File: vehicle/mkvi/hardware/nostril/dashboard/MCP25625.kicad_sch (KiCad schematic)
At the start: 9 parts, among them U2 MCP25625-x-SS, Y1 Crystal_12MHz

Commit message: Final Dashboard Schematic
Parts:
- removed Y1: Crystal_12MHz, footprints:Crystal_SMD_FA238, symbol formula:Crystal_12MHz
- added Y1: Crystal_8MHz_12pF, XTAL_ECS-240-8-33-AGN-TR, symbol formula:Crystal_8MHz_12pF
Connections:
- net GND: now also Y1.2, Y1.4
- net at C7.1, U2.9 (OSC1): now also Y1.1
- net at C8.1, U2.8 (OSC2): now also Y1.3
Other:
- note removed: "Upload actual digikey part This is a placeholder crystal"
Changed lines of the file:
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@@
+    (stroke (width 0) (type default) (color 0 0 0 0))
+  )
+  (wire (pts (xy 156.845 120.015) (xy 151.13 120.015))
     (stroke (width 0) (type default) (color 0 0 0 0))
   )
@@
     (stroke (width 0) (type default) (color 0 0 0 0))
   )
-  (wire (pts (xy 158.115 120.015) (xy 151.13 120.015))
-    (stroke (width 0) (type default) (color 0 0 0 0))
-  )
   (wire (pts (xy 164.465 107.315) (xy 164.465 107.95))
     (stroke (width 0) (type default) (color 0 0 0 0))
@@
     (stroke (width 0) (type default) (color 0 0 0 0))
   )
+  (wire (pts (xy 160.655 114.935) (xy 160.655 107.315))
+    (stroke (width 0) (type default) (color 0 0 0 0))
+  )
   (wire (pts (xy 151.13 120.015) (xy 151.13 126.365))
     (stroke (width 0) (type default) (color 0 0 0 0))
@@
     (stroke (width 0) (type default) (color 0 0 0 0))
   )
-  (wire (pts (xy 160.655 116.205) (xy 160.655 107.315))
-    (stroke (width 0) (type default) (color 0 0 0 0))
-  )
   (wire (pts (xy 115.57 93.345) (xy 91.44 93.345))
     (stroke (width 0) (type default) (color 0 0 0 0))
   )
-  (wire (pts (xy 171.45 120.015) (xy 163.195 120.015))
+  (wire (pts (xy 171.45 120.015) (xy 164.465 120.015))
     (stroke (width 0) (type default) (color 0 0 0 0))
   )
@@
     (stroke (width 0) (type default) (color 0 0 0 0))
   )
-  (wire (pts (xy 160.655 123.825) (xy 160.655 133.985))
-    (stroke (width 0) (type default) (color 0 0 0 0))
-  )
   (wire (pts (xy 107.95 53.975) (xy 107.95 55.245))
     (stroke (width 0) (type default) (color 0 0 0 0))
@@
     (stroke (width 0) (type default) (color 0 0 0 0))
   )
+  (wire (pts (xy 160.655 125.095) (xy 160.655 133.985))
+    (stroke (width 0) (type default) (color 0 0 0 0))
+  )
   (wire (pts (xy 106.68 83.185) (xy 115.57 83.185))
     (stroke (width 0) (type default) (color 0 0 0 0))
-  )
-  (text "Upload actual digikey part\nThis is a placeholder crystal"
-    (at 170.815 116.205 0)
-    (effects (font (size 0.5 0.5)) (justify right bottom))
   )
   (text "Crystal: 12pF, 8 MHz\nPin Load Capacitance (assumed: 5pF)\n\nCL= C1*C2/(C1+C2)\nC1=C2\n(C1^2)/2C1 + 5pF = 12 pF\nC1 = 14 pF\n\nTo do: Add footprint for 14 pF capacitor"
@@
     (effects (font (size 1.27 1.27)) (justify right bottom))
   )
-  (label "CAN_+" (at 158.115 73.025 0)
-    (effects (font (size 1.27 1.27)) (justify left bottom))
-  )
   (label "MOSI" (at 115.57 83.185 180)
     (effects (font (size 1.27 1.27)) (justify right bottom))
@@
     (effects (font (size 1.27 1.27)) (justify right bottom))
   )
-  (label "CAN_-" (at 158.115 80.645 0)
-    (effects (font (size 1.27 1.27)) (justify left bottom))
-  )
   (hierarchical_label "~{TX1RTS}" (shape output) (at 106.68 100.965 180)
     (effects (font (size 1.27 1.27)) (justify right))
@@
   (hierarchical_label "~{RX0BF}" (shape input) (at 106.68 108.585 180)
     (effects (font (size 1.27 1.27)) (justify right))
+  )
+  (hierarchical_label "CAN_-" (shape output) (at 158.115 80.645 0)
+    (effects (font (size 1.27 1.27)) (justify left))
+  )
+  (hierarchical_label "CAN_+" (shape output) (at 158.115 73.025 0)
+    (effects (font (size 1.27 1.27)) (justify left))
   )
   (hierarchical_label "SCK" (shape input) (at 106.68 80.645 180)
@@
     )
     (pin "1")
+  )
+  (symbol (lib_id "formula:Crystal_8MHz_12pF") (at 160.655 120.015 0) (unit 1)
+    (in_bom yes) (on_board yes)
+    (property "Reference" "Y1" (id 0) (at 156.21 116.205 0))
+    (property "Value" "Crystal_8MHz_12pF" (id 1) (at 161.29 126.365 0))
+    (property "Footprint" "XTAL_ECS-240-8-33-AGN-TR" (id 2) (at 221.615 99.695 0)
+      (effects (font (size 1.27 1.27)) (justify left bottom) hide)
+    )
+    (property "Datasheet" "https://ecsxtal.com/store/pdf/ecx-32.pdf" (id 3) (at 160.655 120.015 0)
+      (effects (font (size 1.27 1.27)) (justify left bottom) hide)
+    )
+    (property "PRICE" "" (id 4) (at 160.655 120.015 0)
+      (effects (font (size 1.27 1.27)) (justify left bottom) hide)
+    )
+    (property "MP" "ECS-80-12-33-JGN-TR" (id 5) (at 202.565 112.395 0)
+      (effects (font (size 1.27 1.27)) (justify left bottom) hide)
+    )
+    (property "PACKAGE" "SMD-4 ECX" (id 6) (at 200.025 114.935 0)
+      (effects (font (size 1.27 1.27)) (justify left bottom) hide)
+    )
+    (property "AVAILABILITY" "Good" (id 7) (at 196.215 108.585 0)
+      (effects (font (size 1.27 1.27)) (justify left bottom) hide)
+    )
+    (property "STANDARD" "Manufacturer recommendations" (id 8) (at 208.915 108.585 0)
+      (effects (font (size 1.27 1.27)) (justify left bottom) hide)
+    )
+    (property "Description" "CRYSTAL 8.0000MHZ 12PF SMD" (id 9) (at 191.135 118.745 0)
+      (effects (font (size 1.27 1.27)) (justify left bottom) hide)
+    )
+    (property "MF" "ECS INC" (id 10) (at 217.805 113.665 0)
+      (effects (font (size 1.27 1.27)) (justify left bottom) hide)
+    )
+    (pin "1")
+    (pin "2")
+    (pin "3")
+    (pin "4")
   )
   (symbol (lib_id "power:GND") (at 151.765 64.135 0) (unit 1)
@@
   )
   (symbol (lib_id "Device:C") (at 151.13 130.175 0) (unit 1)
-    (in_bom yes) (on_board yes) (fields_autoplaced)
-    (property "Reference" "C7" (id 0) (at 154.94 128.9049 0)
-      (effects (font (size 1.27 1.27)) (justify left))
-    )
-    (property "Value" "14pF" (id 1) (at 154.94 131.4449 0)
+    (in_bom yes) (on_board yes)
+    (property "Reference" "C7" (id 0) (at 145.415 128.905 0)
+      (effects (font (size 1.27 1.27)) (justify left))
+    )
+    (property "Value" "14pF" (id 1) (at 143.51 131.445 0)
       (effects (font (size 1.27 1.27)) (justify left))
     )
@@
     (pin "1")
   )
-  (symbol (lib_id "formula:Crystal_12MHz") (at 160.655 120.015 0) (mirror y) (unit 1)
-    (in_bom yes) (on_board yes)
-    (property "Reference" "Y1" (id 0) (at 158.115 116.84 0))
-    (property "Value" "Crystal_12MHz" (id 1) (at 160.655 124.46 0))
-    (property "Footprint" "footprints:Crystal_SMD_FA238" (id 2) (at 161.925 118.11 0)
-      (effects (font (size 1.27 1.27)) hide)
-    )
-    (property "Datasheet" "https://ecsxtal.com/store/pdf/ecx-32.pdf" (id 3) (at 159.385 115.57 0)
-      (effects (font (size 1.27 1.27)) hide)
-    )
-    (property "MFN" "DK" (id 4) (at 160.655 120.015 0)
-      (effects (font (size 1.524 1.524)) hide)
-    )
-    (property "MPN" "ECS-120-20-33-CKM-TR" (id 5) (at 160.655 120.015 0)
-      (effects (font (size 1.524 1.524)) hide)
-    )
-    (property "PurchasingLink" "https://www.digikey.com/en/products/detail/ecs-inc/ECS-120-20-33-CKM-TR/2781815" (id 6) (at 160.655 120.015 0)
-      (effects (font (size 1.524 1.524)) hide)
-    )
-    (pin "1")
-    (pin "2")
-    (pin "3")
-    (pin "4")
-  )
   (symbol (lib_id "formula:R_120") (at 151.13 76.835 0) (mirror y) (unit 1)

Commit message: Making sure changes are saved
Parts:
- Y1: value Crystal_8MHz_12pF -> (none); footprint XTAL_ECS-240-8-33-AGN-TR -> (none)
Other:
- note added: "Crystal: 12pF, 8 MHz Pin Load Capacitance (assumed: 5pF) CL= C7*C8/(C7+C8) C7=C8 (C7^2)/2C7 + 5pF = 12 pF C7 = 14 pF To do: Add footprint for 14 pF capacitor"
- note removed: "Crystal: 12pF, 8 MHz Pin Load Capacitance (assumed: 5pF) CL= C1*C2/(C1+C2) C1=C2 (C1^2)/2C1 + 5pF = 12 pF C1 = 14 pF To do: Add footprint for 14 pF capacitor"
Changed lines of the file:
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@@
     (stroke (width 0) (type default) (color 0 0 0 0))
   )
-  (text "Crystal: 12pF, 8 MHz\nPin Load Capacitance (assumed: 5pF)\n\nCL= C1*C2/(C1+C2)\nC1=C2\n(C1^2)/2C1 + 5pF = 12 pF\nC1 = 14 pF\n\nTo do: Add footprint for 14 pF capacitor"
+  (text "Crystal: 12pF, 8 MHz\nPin Load Capacitance (assumed: 5pF)\n\nCL= C7*C8/(C7+C8)\nC7=C8\n(C7^2)/2C7 + 5pF = 12 pF\nC7 = 14 pF\n\nTo do: Add footprint for 14 pF capacitor"
     (at 174.625 121.92 0)
     (effects (font (size 1.27 1.27)) (justify left bottom))
@@
     (in_bom yes) (on_board yes)
     (property "Reference" "Y1" (id 0) (at 156.21 116.205 0))
-    (property "Value" "Crystal_8MHz_12pF" (id 1) (at 161.29 126.365 0))
-    (property "Footprint" "XTAL_ECS-240-8-33-AGN-TR" (id 2) (at 221.615 99.695 0)
+    (property "Value" "" (id 1) (at 161.29 126.365 0))
+    (property "Footprint" "" (id 2) (at 221.615 99.695 0)
       (effects (font (size 1.27 1.27)) (justify left bottom) hide)
     )

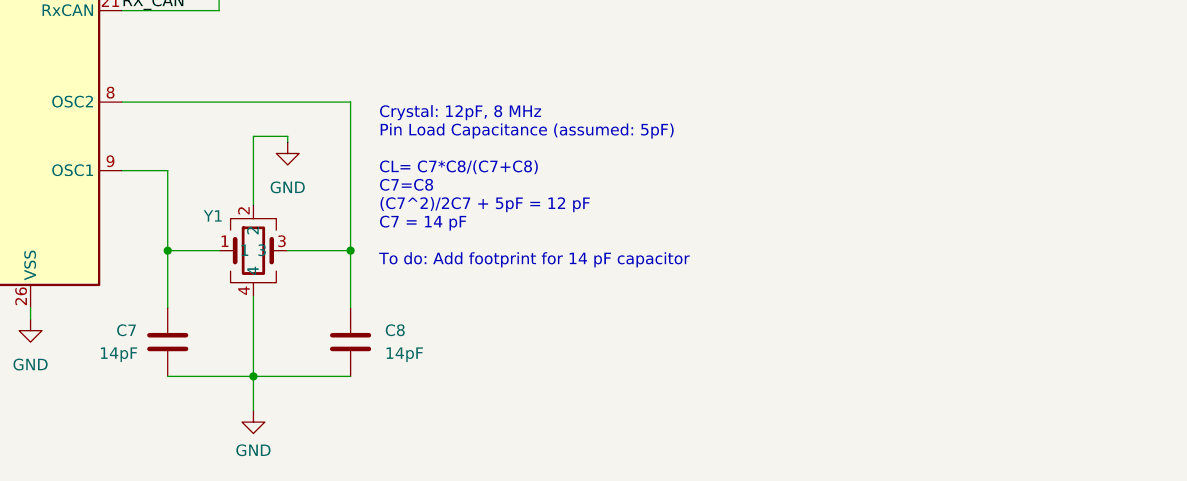
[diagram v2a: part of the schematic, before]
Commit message: Edited text beside crystal attached to MCP25625 chip
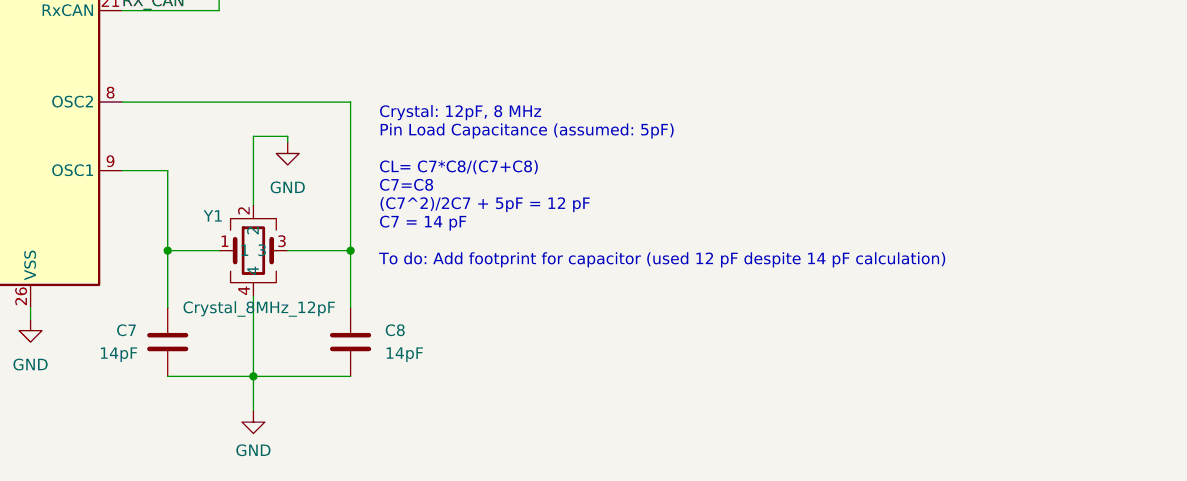
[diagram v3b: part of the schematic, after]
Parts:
- Y1: value (none) -> Crystal_8MHz_12pF; footprint (none) -> XTAL_ECS-240-8-33-AGN-TR
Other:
- note added: "Crystal: 12pF, 8 MHz Pin Load Capacitance (assumed: 5pF) CL= C7*C8/(C7+C8) C7=C8 (C7^2)/2C7 + 5pF = 12 pF C7 = 14 pF To do: Add footprint for capacitor (used 12 pF despite 14 pF calculation)"
- note removed: "Crystal: 12pF, 8 MHz Pin Load Capacitance (assumed: 5pF) CL= C7*C8/(C7+C8) C7=C8 (C7^2)/2C7 + 5pF = 12 pF C7 = 14 pF To do: Add footprint for 14 pF capacitor"
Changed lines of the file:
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@@
     (stroke (width 0) (type default) (color 0 0 0 0))
   )
-  (text "Crystal: 12pF, 8 MHz\nPin Load Capacitance (assumed: 5pF)\n\nCL= C7*C8/(C7+C8)\nC7=C8\n(C7^2)/2C7 + 5pF = 12 pF\nC7 = 14 pF\n\nTo do: Add footprint for 14 pF capacitor"
+  (text "Crystal: 12pF, 8 MHz\nPin Load Capacitance (assumed: 5pF)\n\nCL= C7*C8/(C7+C8)\nC7=C8\n(C7^2)/2C7 + 5pF = 12 pF\nC7 = 14 pF\n\nTo do: Add footprint for capacitor (used 12 pF despite 14 pF calculation)"
     (at 174.625 121.92 0)
     (effects (font (size 1.27 1.27)) (justify left bottom))
@@
     (in_bom yes) (on_board yes)
     (property "Reference" "Y1" (id 0) (at 156.21 116.205 0))
-    (property "Value" "" (id 1) (at 161.29 126.365 0))
-    (property "Footprint" "" (id 2) (at 221.615 99.695 0)
+    (property "Value" "Crystal_8MHz_12pF" (id 1) (at 161.29 126.365 0))
+    (property "Footprint" "XTAL_ECS-240-8-33-AGN-TR" (id 2) (at 221.615 99.695 0)
       (effects (font (size 1.27 1.27)) (justify left bottom) hide)
     )

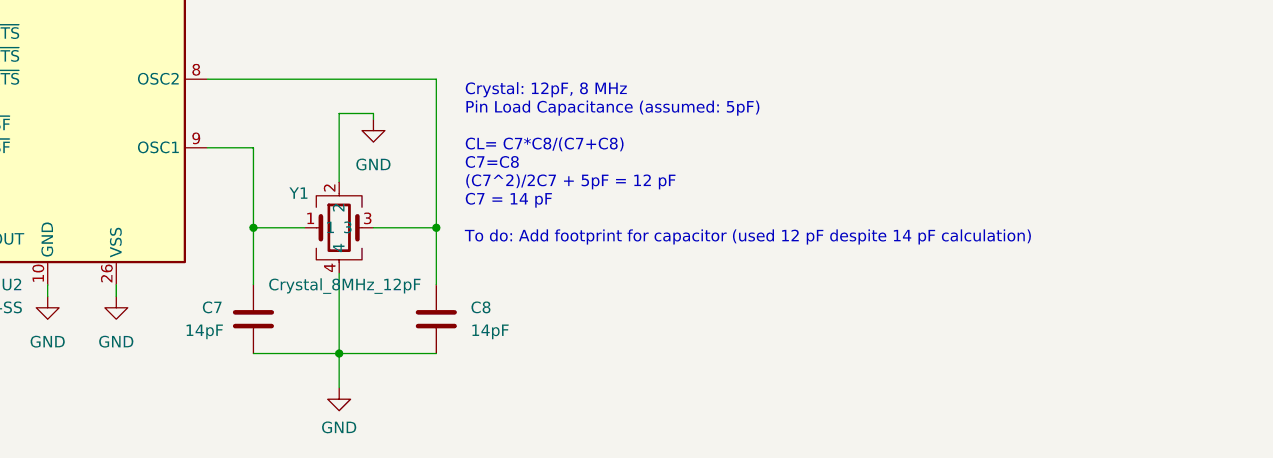
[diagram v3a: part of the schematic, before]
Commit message: Added 14 pF capacitor for crystal to the formula library, ensured every symbol is from the formula library
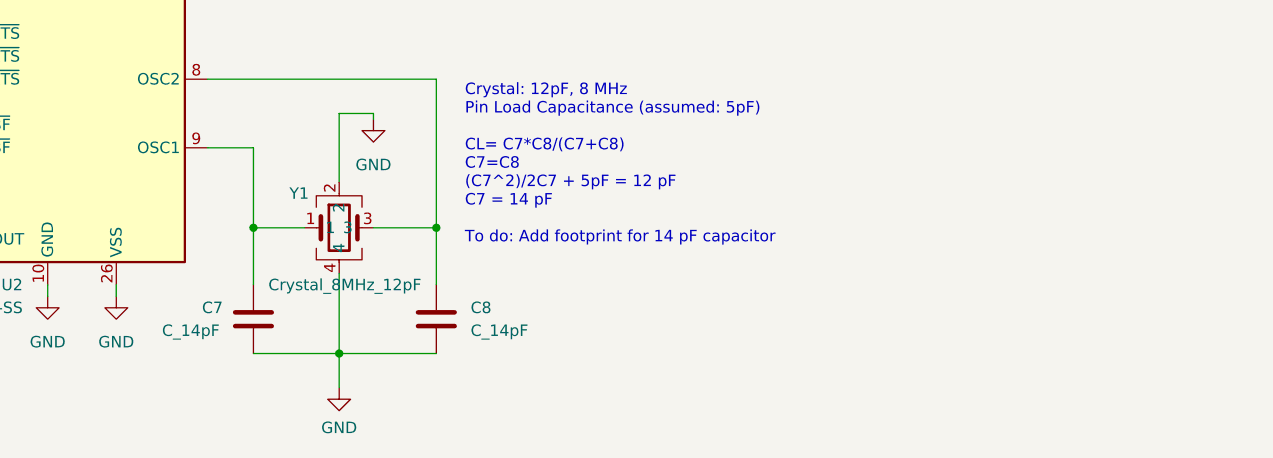
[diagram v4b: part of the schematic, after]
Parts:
- removed C7, C8: 14pF, symbol Device:C
- added C7, C8: C_14pF, footprints:C_0805_OEM, symbol formula:C_14pF
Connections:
- net GND: now also C7.2, C8.2
- net at U2.9 (OSC1), Y1.1: now also C7.1
- net at U2.8 (OSC2), Y1.3: now also C8.1
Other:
- note added: "Crystal: 12pF, 8 MHz Pin Load Capacitance (assumed: 5pF) CL= C7*C8/(C7+C8) C7=C8 (C7^2)/2C7 + 5pF = 12 pF C7 = 14 pF To do: Add footprint for 14 pF capacitor"
- note removed: "Crystal: 12pF, 8 MHz Pin Load Capacitance (assumed: 5pF) CL= C7*C8/(C7+C8) C7=C8 (C7^2)/2C7 + 5pF = 12 pF C7 = 14 pF To do: Add footprint for capacitor (used 12 pF despite 14 pF calculation)"
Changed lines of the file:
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@@
     (stroke (width 0) (type default) (color 0 0 0 0))
   )
-  (text "Crystal: 12pF, 8 MHz\nPin Load Capacitance (assumed: 5pF)\n\nCL= C7*C8/(C7+C8)\nC7=C8\n(C7^2)/2C7 + 5pF = 12 pF\nC7 = 14 pF\n\nTo do: Add footprint for capacitor (used 12 pF despite 14 pF calculation)"
+  (text "Crystal: 12pF, 8 MHz\nPin Load Capacitance (assumed: 5pF)\n\nCL= C7*C8/(C7+C8)\nC7=C8\n(C7^2)/2C7 + 5pF = 12 pF\nC7 = 14 pF\n\nTo do: Add footprint for 14 pF capacitor"
     (at 174.625 121.92 0)
     (effects (font (size 1.27 1.27)) (justify left bottom))
@@
     (pin "1")
   )
+  (symbol (lib_id "formula:C_14pF") (at 171.45 130.175 0) (unit 1)
+    (in_bom yes) (on_board yes) (fields_autoplaced)
+    (property "Reference" "C8" (id 0) (at 175.26 128.9049 0)
+      (effects (font (size 1.27 1.27)) (justify left))
+    )
+    (property "Value" "C_14pF" (id 1) (at 175.26 131.4449 0)
+      (effects (font (size 1.27 1.27)) (justify left))
+    )
+    (property "Footprint" "footprints:C_0805_OEM" (id 2) (at 172.4152 133.985 0)
+      (effects (font (size 1.27 1.27)) hide)
+    )
+    (property "Datasheet" "https://search.murata.co.jp/Ceramy/image/img/A01X/G101/ENG/GQM2195C2E140JB12-01.pdf" (id 3) (at 162.56 113.665 0)
+      (effects (font (size 1.27 1.27)) hide)
+    )
+    (property "MFN" "Murata Electronics" (id 4) (at 171.45 130.175 0)
+      (effects (font (size 1.27 1.27)) hide)
+    )
+    (property "MPN" "GQM2195C2E140JB12D" (id 5) (at 170.18 130.175 0)
+      (effects (font (size 1.27 1.27)) hide)
+    )
+    (property "Purchasing Link" "https://www.digikey.com/en/products/detail/murata-electronics/GQM2195C2E140JB12D/13401886" (id 6) (at 171.45 130.175 0)
+      (effects (font (size 1.27 1.27)) hide)
+    )
+    (property "PurchasingLink" "https://www.digikey.com/products/en?keywords=478-3352-1-ND" (id 7) (at 182.245 117.475 0)
+      (effects (font (size 1.524 1.524)) hide)
+    )
+    (pin "1")
+    (pin "2")
+  )
   (symbol (lib_id "formula:C_0.1uF") (at 144.78 62.23 270) (unit 1)
     (in_bom yes) (on_board yes)
@@
     (pin "2")
   )
-  (symbol (lib_id "Device:C") (at 151.13 130.175 0) (unit 1)
+  (symbol (lib_id "formula:C_14pF") (at 151.13 130.175 0) (unit 1)
     (in_bom yes) (on_board yes)
     (property "Reference" "C7" (id 0) (at 145.415 128.905 0)
       (effects (font (size 1.27 1.27)) (justify left))
     )
-    (property "Value" "14pF" (id 1) (at 143.51 131.445 0)
-      (effects (font (size 1.27 1.27)) (justify left))
-    )
-    (property "Footprint" "" (id 2) (at 152.0952 133.985 0)
-      (effects (font (size 1.27 1.27)) hide)
-    )
-    (property "Datasheet" "~" (id 3) (at 151.13 130.175 0)
-      (effects (font (size 1.27 1.27)) hide)
+    (property "Value" "C_14pF" (id 1) (at 140.97 131.445 0)
+      (effects (font (size 1.27 1.27)) (justify left))
+    )
+    (property "Footprint" "footprints:C_0805_OEM" (id 2) (at 152.0952 133.985 0)
+      (effects (font (size 1.27 1.27)) hide)
+    )
+    (property "Datasheet" "https://search.murata.co.jp/Ceramy/image/img/A01X/G101/ENG/GQM2195C2E140JB12-01.pdf" (id 3) (at 142.24 113.665 0)
+      (effects (font (size 1.27 1.27)) hide)
+    )
+    (property "MFN" "Murata Electronics" (id 4) (at 151.13 130.175 0)
+      (effects (font (size 1.27 1.27)) hide)
+    )
+    (property "MPN" "GQM2195C2E140JB12D" (id 5) (at 149.86 130.175 0)
+      (effects (font (size 1.27 1.27)) hide)
+    )
+    (property "Purchasing Link" "https://www.digikey.com/en/products/detail/murata-electronics/GQM2195C2E140JB12D/13401886" (id 6) (at 151.13 130.175 0)
+      (effects (font (size 1.27 1.27)) hide)
+    )
+    (property "PurchasingLink" "https://www.digikey.com/products/en?keywords=478-3352-1-ND" (id 7) (at 161.925 117.475 0)
+      (effects (font (size 1.524 1.524)) hide)
     )
     (pin "1")
@@
     )
     (pin "1")
-    (pin "2")
-  )
-  (symbol (lib_id "Device:C") (at 171.45 130.175 0) (unit 1)
-    (in_bom yes) (on_board yes) (fields_autoplaced)
-    (property "Reference" "C8" (id 0) (at 175.26 128.9049 0)
-      (effects (font (size 1.27 1.27)) (justify left))
-    )
-    (property "Value" "14pF" (id 1) (at 175.26 131.4449 0)
-      (effects (font (size 1.27 1.27)) (justify left))
-    )
-    (property "Footprint" "" (id 2) (at 172.4152 133.985 0)
-      (effects (font (size 1.27 1.27)) hide)
-    )
-    (property "Datasheet" "~" (id 3) (at 171.45 130.175 0)
-      (effects (font (size 1.27 1.27)) hide)
-    )
-    (pin "1")

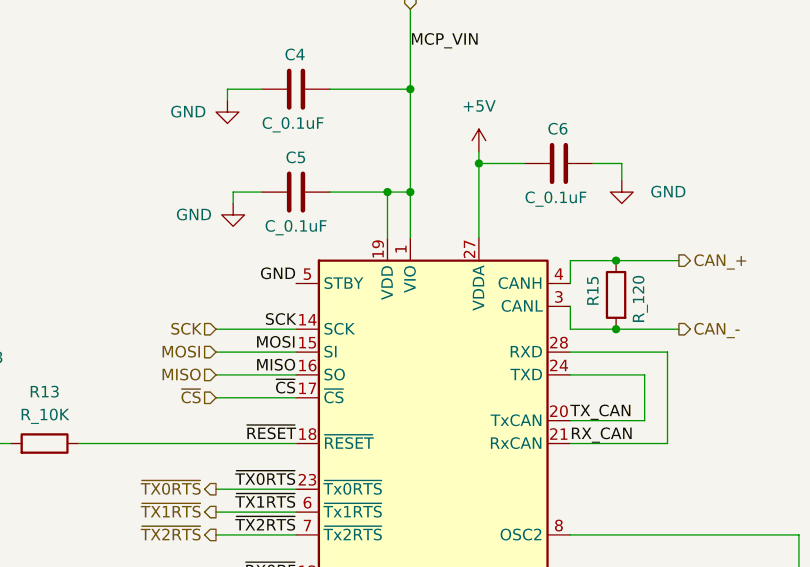
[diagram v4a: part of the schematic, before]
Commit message: Address PR comments, 0603 passives, panel light resistors
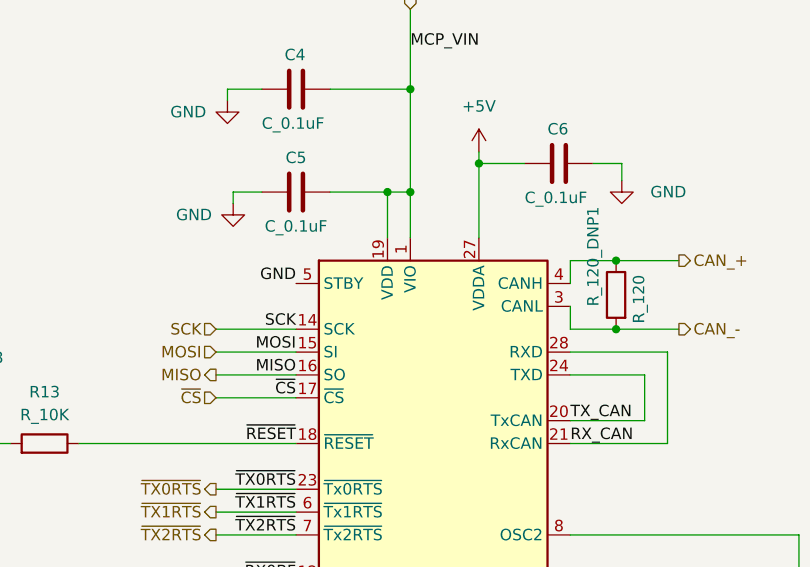
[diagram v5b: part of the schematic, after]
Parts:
- renumbered R15 to R_120_DNP1
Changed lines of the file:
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@@
     (effects (font (size 1.27 1.27)) (justify right))
   )
-  (hierarchical_label "MISO" (shape input) (at 106.68 85.725 180)
+  (hierarchical_label "MISO" (shape output) (at 106.68 85.725 180)
     (effects (font (size 1.27 1.27)) (justify right))
   )
@@
   (symbol (lib_id "formula:R_120") (at 151.13 76.835 0) (mirror y) (unit 1)
     (in_bom yes) (on_board yes)
-    (property "Reference" "R15" (id 0) (at 148.59 78.105 90)
-      (effects (font (size 1.27 1.27)) (justify left))
-    )
+    (property "Reference" "R_120_DNP1" (id 0) (at 148.59 78.105 90)
+      (effects (font (size 1.27 1.27)) (justify left))
+    )
